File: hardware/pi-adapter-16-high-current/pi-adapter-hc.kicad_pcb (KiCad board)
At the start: 4 copper layers, 64 x 56 mm, 38 parts, among them J1 Conn_02x02_Odd_Even, P1 CONN_01X04, P10 CONN_01X04, P11 CONN_01X04, P12 CONN_01X04, P13 CONN_01X04, P14 CONN_01X04, P15 CONN_01X04, P16 CONN_01X04, P17 5V, P2 CONN_01X04, P20 Pi-GPIO, P21 I2C, P22 System SPI, P23 UART, P3 CONN_01X04, P30 +5V, P31 GND, P4 CONN_01X04, P40 CONN_01X01, P41 CONN_01X01, P43 CONN_01X01, P5 CONN_01X04, P6 CONN_01X04, P7 CONN_01X04, P8 CONN_01X04, P9 CONN_01X04, U1 74HC245, U2 74HC245, U3 74HC245, U4 74HC245

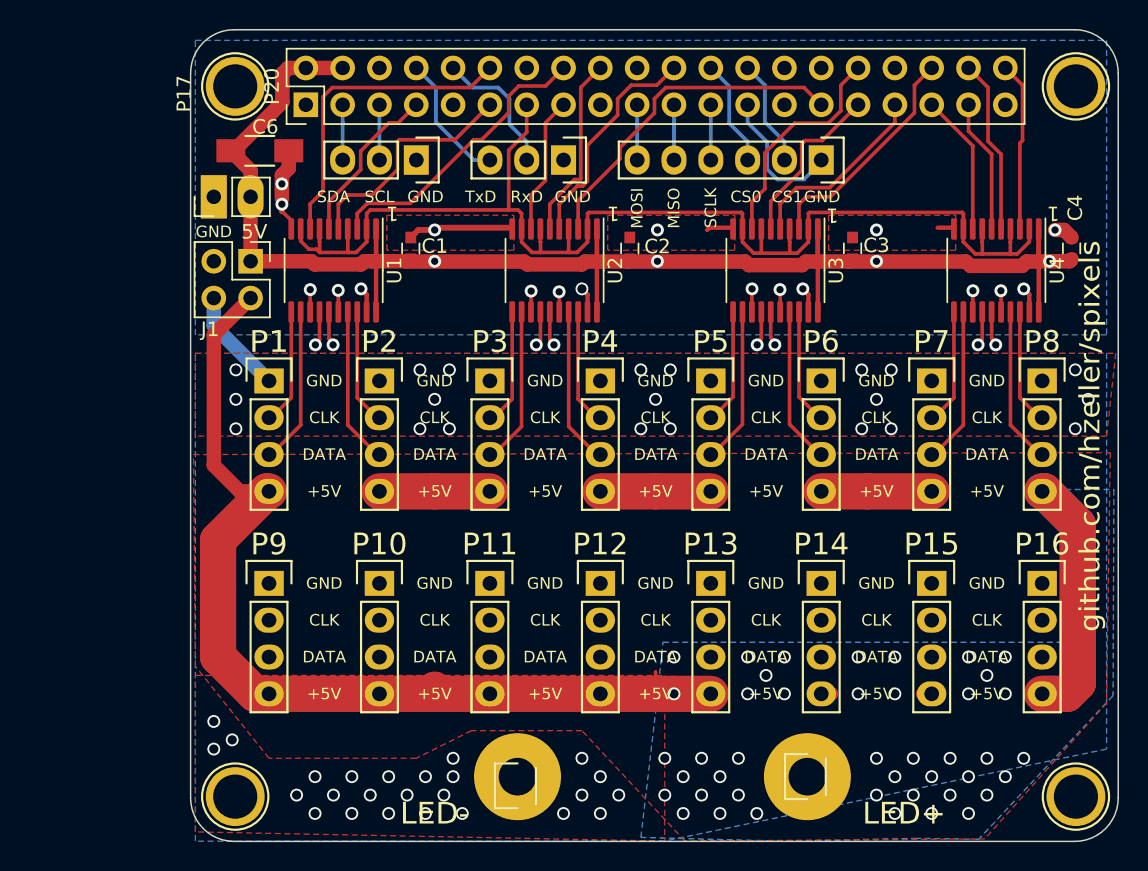
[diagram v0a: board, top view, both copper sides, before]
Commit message: Separate LED power input for upper and lower bank.
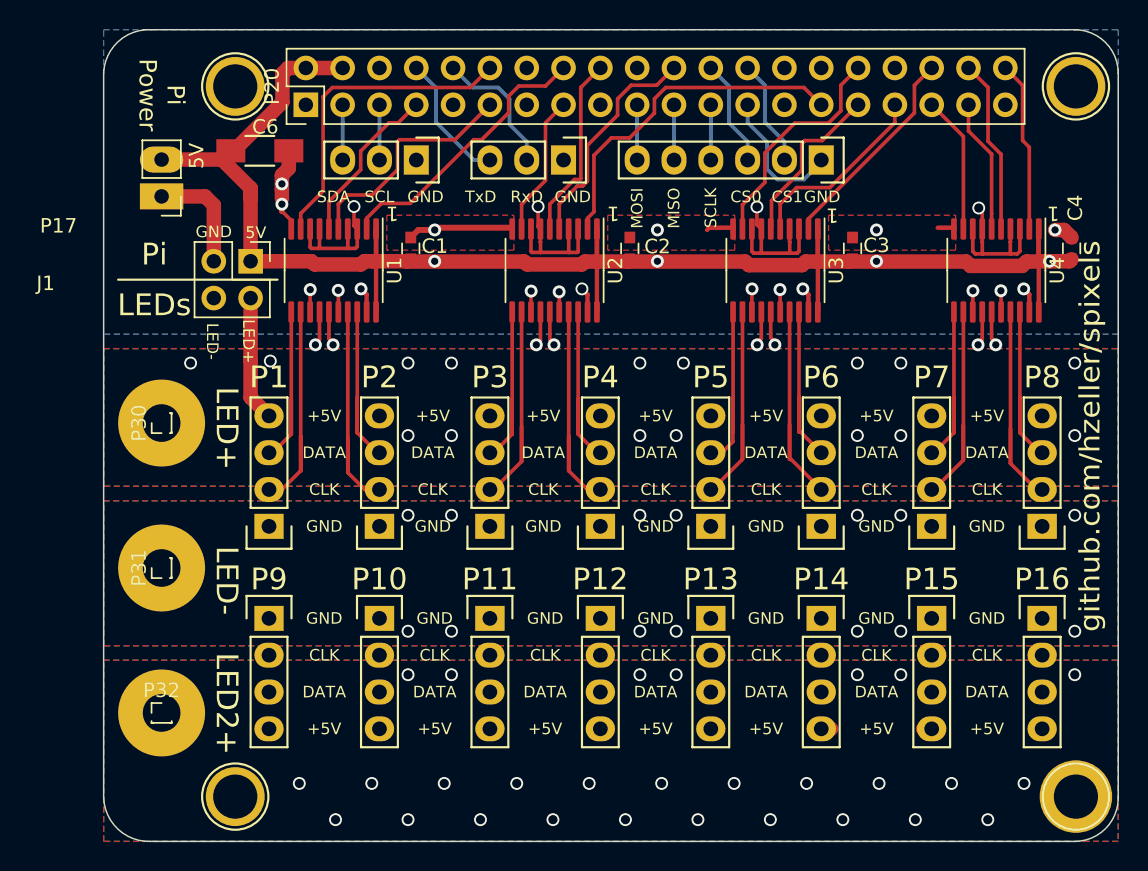
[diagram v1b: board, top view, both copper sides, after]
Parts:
- added P32: +5V, Connector_PinHeader_1.00mm:PinHeader_1x01_P1.00mm_Vertical, F.Cu at (98.0, 85.1)
- P30, P31: footprint Pin_Headers:Pin_Header_Straight_1x01 -> Connector_PinHeader_1.00mm:PinHeader_1x01_P1.00mm_Vertical
- moved P30 50.8 mm to (98.0, 65.1)
- moved P31 28.8 mm to (98.0, 75.1)
- moved P1 10.0 mm to (105.4, 72.3), turned to 180 degrees
- moved P2 10.0 mm to (113.0, 72.3), turned to 180 degrees
- moved P3 10.0 mm to (120.7, 72.3), turned to 180 degrees
- moved P4 10.0 mm to (128.3, 72.3), turned to 180 degrees
- moved P5 10.0 mm to (135.9, 72.3), turned to 180 degrees
- moved P6 10.0 mm to (143.5, 72.3), turned to 180 degrees
- moved P7 10.0 mm to (151.1, 72.3), turned to 180 degrees
- moved P8 10.0 mm to (158.8, 72.3), turned to 180 degrees
- moved P17 3.60 mm to (98.0, 49.5), turned to 180 degrees
- moved P10 2.41 mm to (113.0, 78.6)
- moved P11 2.41 mm to (120.7, 78.6)
- moved P12 2.41 mm to (128.3, 78.6)
- moved P13 2.41 mm to (135.9, 78.6)
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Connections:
- P1 pad 3: Net-(P1-Pad3) -> Net-(U1-Pad11)
- P10 pad 4: LED-Power+ -> LED-Power2+
- P11 pad 4: LED-Power+ -> LED-Power2+
- P12 pad 4: LED-Power+ -> LED-Power2+
- P13 pad 4: LED-Power+ -> LED-Power2+
- P14 pad 4: LED-Power+ -> LED-Power2+
- P15 pad 4: LED-Power+ -> LED-Power2+
- P16 pad 4: LED-Power+ -> LED-Power2+
- P2 pad 3: Net-(P2-Pad3) -> Net-(U1-Pad18)
- P20 pad 1: no_connect_63 -> no_connect_64
- P20 pad 17: no_connect_64 -> no_connect_65
- P20 pad 27: no_connect_65 -> no_connect_66
- P20 pad 28: no_connect_66 -> no_connect_67
- P20 pad 9: no_connect_67 -> no_connect_68
- P3 pad 2: Net-(P3-Pad2) -> Net-(U2-Pad12)
- P3 pad 3: Net-(P3-Pad3) -> Net-(U2-Pad11)
- P5 pad 2: Net-(P5-Pad2) -> Net-(U3-Pad12)
- P5 pad 3: Net-(P5-Pad3) -> Net-(U3-Pad11)
- P6 pad 2: Net-(P6-Pad2) -> Net-(U3-Pad17)
- P6 pad 3: Net-(P6-Pad3) -> Net-(U3-Pad18)
- P9 pad 4: LED-Power+ -> LED-Power2+
- U1 pad 11: Net-(P1-Pad2) -> Net-(U1-Pad11)
- U1 pad 12: Net-(P1-Pad3) -> Net-(P1-Pad2)
- U1 pad 17: Net-(P2-Pad3) -> Net-(P2-Pad2)
- U1 pad 18: Net-(P2-Pad2) -> Net-(U1-Pad18)
- U1 pad 2: clock -> D4
- U1 pad 3: D4 -> clock
- U1 pad 8: D1 -> clock
- U1 pad 9: clock -> D1
- U2 pad 11: Net-(P3-Pad2) -> Net-(U2-Pad11)
- U2 pad 12: Net-(P3-Pad3) -> Net-(U2-Pad12)
- U2 pad 17: Net-(P4-Pad3) -> Net-(P4-Pad2)
- U2 pad 18: Net-(P4-Pad2) -> Net-(P4-Pad3)
- U2 pad 2: clock -> D8
- U2 pad 3: D8 -> clock
- U2 pad 8: D5 -> clock
- U2 pad 9: clock -> D5
- U3 pad 11: Net-(P5-Pad2) -> Net-(U3-Pad11)
- U3 pad 12: Net-(P5-Pad3) -> Net-(U3-Pad12)
- U3 pad 17: Net-(P6-Pad3) -> Net-(U3-Pad17)
- U3 pad 18: Net-(P6-Pad2) -> Net-(U3-Pad18)
- U3 pad 2: clock -> D12
- U3 pad 3: D12 -> clock
- U3 pad 8: D9 -> clock
- U3 pad 9: clock -> D9
- U4 pad 11: Net-(P7-Pad2) -> Net-(P7-Pad3)
- U4 pad 12: Net-(P7-Pad3) -> Net-(P7-Pad2)
- U4 pad 17: Net-(P8-Pad3) -> Net-(P8-Pad2)
- U4 pad 18: Net-(P8-Pad2) -> Net-(P8-Pad3)
- U4 pad 2: clock -> D16
- U4 pad 3: D16 -> clock
- U4 pad 8: D13 -> clock
- U4 pad 9: clock -> D13
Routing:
- net LED-Power+: track 128.1 -> 8.65 mm, vias 43 -> 16
- net Net-(U3-Pad17): track 0.00 -> 15.7 mm
- net Net-(U3-Pad12): track 0.00 -> 15.7 mm
- net Net-(U2-Pad12): track 0.00 -> 15.7 mm
- net Net-(U1-Pad11): track 0.00 -> 13.7 mm
- net LED-Power-: track 7.29 -> 20.9 mm, vias 46 -> 14
- net Net-(U3-Pad11): track 0.00 -> 13.3 mm
- net Net-(U3-Pad18): track 0.00 -> 12.9 mm
- net Net-(U2-Pad11): track 0.00 -> 12.9 mm
- net Net-(U1-Pad18): track 0.00 -> 12.8 mm
- net Net-(P6-Pad3): track 10.7 -> 0.00 mm
- net Net-(P5-Pad3): track 10.7 -> 0.00 mm
- net Net-(P2-Pad3): track 10.7 -> 0.00 mm
- net Net-(P1-Pad3): track 10.7 -> 0.00 mm
- net Net-(P3-Pad3): track 10.7 -> 0.00 mm
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- added copper zone on B.Cu, net LED-Power2+
- added copper zone on F.Cu, net LED-Power2+
- added copper zone on In1.Cu, net LED-Power2+
- removed copper zone on In2.Cu, net LED-Power-
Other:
- board size 64 x 56 mm -> 70 x 56 mm
- board text added: "5V"
- board text added: "LED2+"
- board text added: "LEDs"
- board text added: "Pi"
- board text added: "Pi Power"

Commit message: Do all clk/data on an inner layer to utilize thicker outer layers for power.
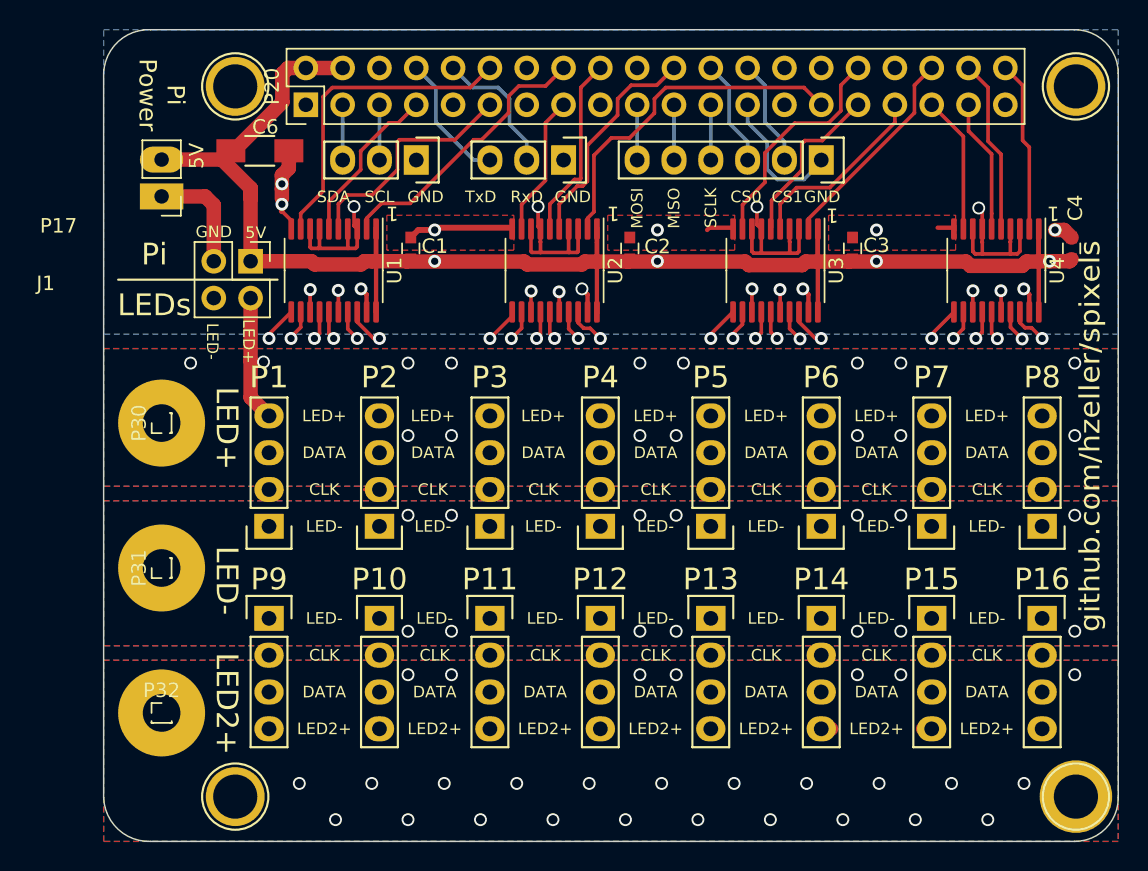
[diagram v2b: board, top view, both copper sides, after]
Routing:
- net Net-(P12-Pad2): track 30.4 -> 28.5 mm
- net Net-(P11-Pad3): track 30.1 -> 28.3 mm
- net Net-(P11-Pad2): track 30.5 -> 28.8 mm
- net Net-(U1-Pad11): track 13.7 -> 12.0 mm, vias 0 -> 1
- net Net-(P12-Pad3): track 30.1 -> 28.4 mm
- net Net-(U3-Pad12): track 15.7 -> 14.2 mm, vias 0 -> 1
- net Net-(P9-Pad3): track 30.1 -> 28.6 mm
- net Net-(P1-Pad2): track 16.2 -> 14.7 mm, vias 0 -> 1
- net Net-(P9-Pad2): track 30.5 -> 29.1 mm
- net Net-(P13-Pad2): track 30.5 -> 29.2 mm
- net Net-(P10-Pad2): track 30.4 -> 29.1 mm
- net Net-(U3-Pad17): track 15.7 -> 14.4 mm, vias 0 -> 1
- net Net-(P16-Pad2): track 30.4 -> 29.1 mm
- net Net-(P7-Pad2): track 15.6 -> 14.3 mm, vias 0 -> 1
- net Net-(P15-Pad3): track 30.1 -> 28.8 mm
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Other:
- board text removed: "+5V"
